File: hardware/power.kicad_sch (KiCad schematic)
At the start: 14 parts, among them J102 USB-C 16P, U103 AP63200WU, U104 CH224K

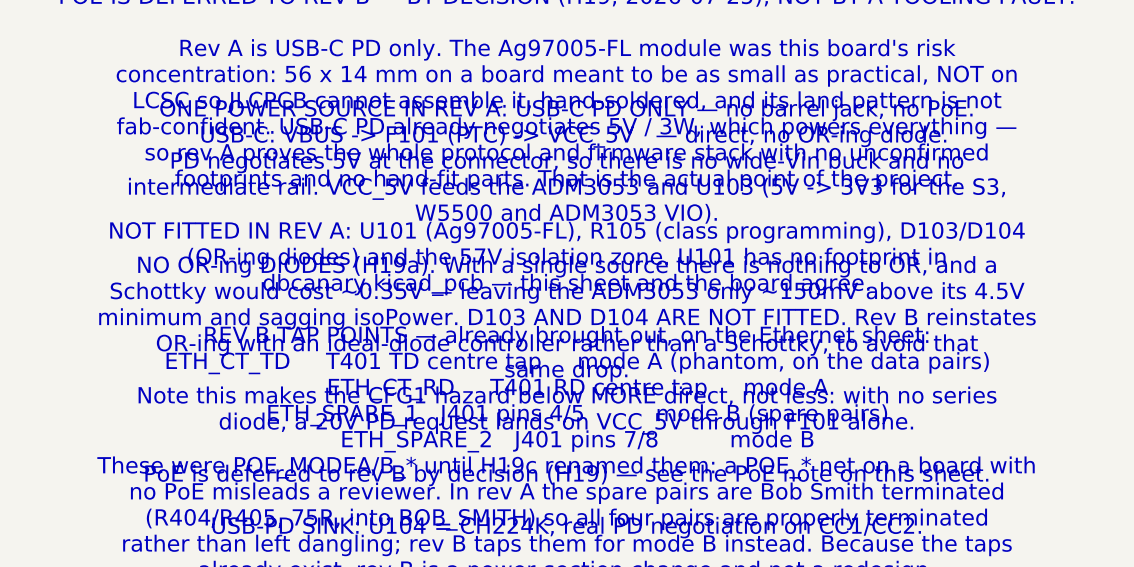
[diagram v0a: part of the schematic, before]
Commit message: CANary: rename, default name in R1, flush switch cover, insert jig
- Renamed dbCANary -> CANary across docs, firmware, tools, enclosure and the
  KiCad project (files and footprint library nickname). The firmware's NVS
  settings namespace keeps its old name so configured units keep their
  settings; the 0.1.0 changelog entry and board #1's bring-up log and test
  record keep the name they were written under.
- A unit is listed in R1 as "CANary" by default, not the R70 factory "db-70".
- The tube's switch cover sits flush in a 1.2 mm pocket in the lid, with a
  lever notch for a small screwdriver. Not interchangeable with 0.1.0 parts.
- Heat-set insert jig for a common 3D-printed insert press: index plate,
  nest and keyed peg, one socket per insert, verified by posing the real
  tube for every socket.

Co-Authored-By: Claude Opus 5.5 <noreply@anthropic.com>
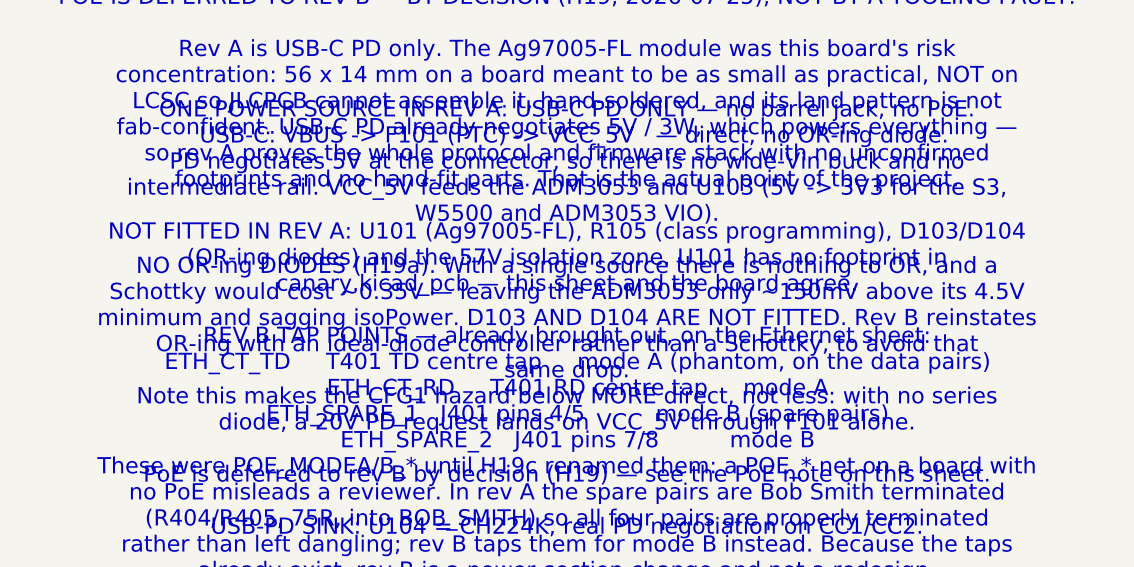
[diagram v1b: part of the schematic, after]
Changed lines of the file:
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@@
         (size 1.8 1.8)))
 )
-  (text "POE IS DEFERRED TO REV B — BY DECISION (H19, 2026-07-25), NOT BY A TOOLING FAULT.\n\nRev A is USB-C PD only. The Ag97005-FL module was this board's risk\nconcentration: 56 x 14 mm on a board meant to be as small as practical, NOT on\nLCSC so JLCPCB cannot assemble it, hand-soldered, and its land pattern is not\nfab-confident. USB-C PD already negotiates 5V / 3W, which powers everything —\nso rev A proves the whole protocol and firmware stack with no unconfirmed\nfootprints and no hand-fit parts. That is the actual point of the project.\n\nNOT FITTED IN REV A: U101 (Ag97005-FL), R105 (class programming), D103/D104\n(OR-ing diodes) and the 57V isolation zone. U101 has no footprint in\ndbcanary.kicad_pcb — this sheet and the board agree.\n\nREV B TAP POINTS — already brought out, on the Ethernet sheet:\n   ETH_CT_TD     T401 TD centre tap     mode A (phantom, on the data pairs)\n   ETH_CT_RD     T401 RD centre tap     mode A\n   ETH_SPARE_1   J401 pins 4/5          mode B (spare pairs)\n   ETH_SPARE_2   J401 pins 7/8          mode B\nThese were POE_MODEA/B_* until H19c renamed them: a POE_* net on a board with\nno PoE misleads a reviewer. In rev A the spare pairs are Bob Smith terminated\n(R404/R405, 75R, into BOB_SMITH) so all four pairs are properly terminated\nrather than left dangling; rev B taps them for mode B instead. Because the taps\nalready exist, rev B is a power-section change and not a redesign.\n\nERC IS CLEAN: zero errors. The six former power_pin_not_driven errors were\nresolved with PWR_FLAG — correctly, not silenced. Rev A's rails genuinely ARE\ndriven, from J102's VBUS pin, which is a passive connector pin: precisely the\ncase PWR_FLAG exists for. Flags sit on VCC_5V, VCC_3V3, GND, VISO, CAN_GND and\nPD_VDD (the last derived through R106, a passive resistor)."
+  (text "POE IS DEFERRED TO REV B — BY DECISION (H19, 2026-07-25), NOT BY A TOOLING FAULT.\n\nRev A is USB-C PD only. The Ag97005-FL module was this board's risk\nconcentration: 56 x 14 mm on a board meant to be as small as practical, NOT on\nLCSC so JLCPCB cannot assemble it, hand-soldered, and its land pattern is not\nfab-confident. USB-C PD already negotiates 5V / 3W, which powers everything —\nso rev A proves the whole protocol and firmware stack with no unconfirmed\nfootprints and no hand-fit parts. That is the actual point of the project.\n\nNOT FITTED IN REV A: U101 (Ag97005-FL), R105 (class programming), D103/D104\n(OR-ing diodes) and the 57V isolation zone. U101 has no footprint in\ncanary.kicad_pcb — this sheet and the board agree.\n\nREV B TAP POINTS — already brought out, on the Ethernet sheet:\n   ETH_CT_TD     T401 TD centre tap     mode A (phantom, on the data pairs)\n   ETH_CT_RD     T401 RD centre tap     mode A\n   ETH_SPARE_1   J401 pins 4/5          mode B (spare pairs)\n   ETH_SPARE_2   J401 pins 7/8          mode B\nThese were POE_MODEA/B_* until H19c renamed them: a POE_* net on a board with\nno PoE misleads a reviewer. In rev A the spare pairs are Bob Smith terminated\n(R404/R405, 75R, into BOB_SMITH) so all four pairs are properly terminated\nrather than left dangling; rev B taps them for mode B instead. Because the taps\nalready exist, rev B is a power-section change and not a redesign.\n\nERC IS CLEAN: zero errors. The six former power_pin_not_driven errors were\nresolved with PWR_FLAG — correctly, not silenced. Rev A's rails genuinely ARE\ndriven, from J102's VBUS pin, which is a passive connector pin: precisely the\ncase PWR_FLAG exists for. Flags sit on VCC_5V, VCC_3V3, GND, VISO, CAN_GND and\nPD_VDD (the last derived through R106, a passive resistor)."
     (at 40 148 0)
     (effects
